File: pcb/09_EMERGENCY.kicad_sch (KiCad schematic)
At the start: 14 parts, among them K1 HF115F-1/5V-H, Q20 AO3400A

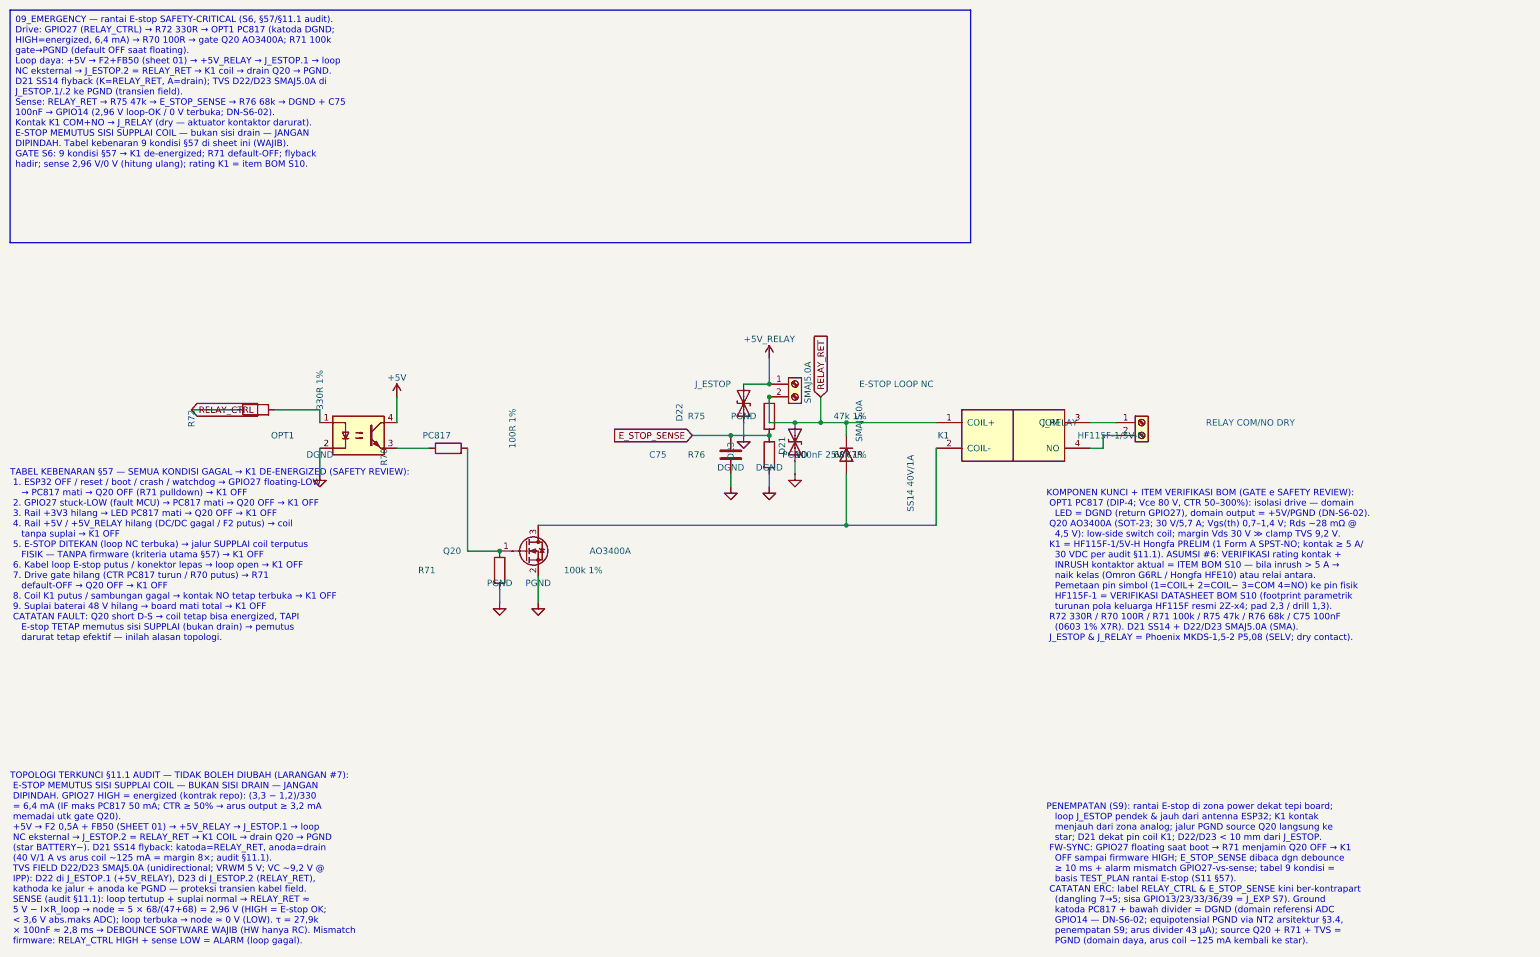
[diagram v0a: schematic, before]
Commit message: pcb: S12 relay-expansion integration + R1/R2 e-stop fixes (schematic + board)
- 09_EMERGENCY: R1 fix (active-LOW drive: R72 high-side from +3V3, OPT1 cathode
  -> RELAY_CTRL, R78 10k pull-up fail-safe) + R2 fix (inverting sense: Q21
  BSS138 + R77 100k divider + R76 revalued 10k pull-up, C75 filter; HIGH=trip
  matches GPIO14 INPUT_PULLUP contract); truth table/docs updated
- NEW 12_RELAY_EXP: F4 1.1A + FB2 -> +5V_RELAY_EXP rail, J_RELAY_EXP 2x03,
  BSS138 I2C shifters Q22/Q23 + R79/R84 4k7, TVS D24/D25 DNP, INT divider
  R82/R83 (PCF8574 module external, 0x20, active-LOW)
- root sch: sheet 12 entry (page 13); plts-custom: +5V_RELAY_EXP symbol
- pro: PWR netclass pattern for +5V_RELAY_EXP
- 01_POWER: C52 22uF->47uF 25V X5R (relay coil dip headroom)
- board: +7 nets, +14 footprints, pad re-netting, placement to 0 structural
  DRC; repaired broken hand-drawn courtyards (M1/U1/K1/J_I2C_EXP) to true
  geometry; U1 antenna keepout respected

ERC: 0 violations (13 sheets). DRC: 0 structural (courtyard/short/keepout/
clearance clean; silk/via/thermal/isolated = post-routing cleanup).
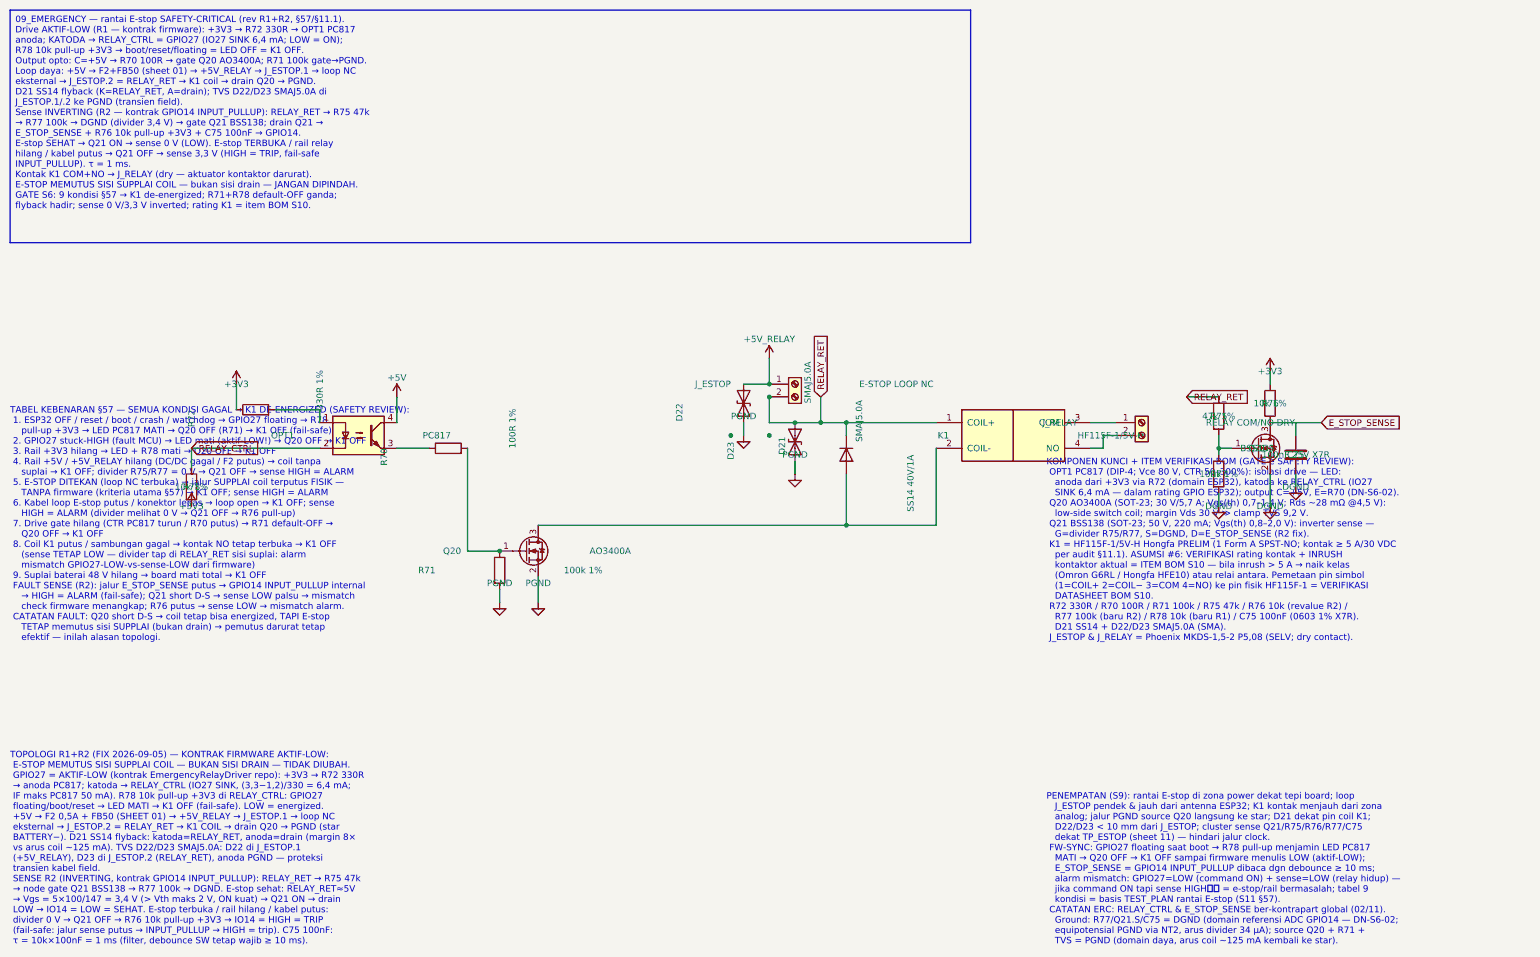
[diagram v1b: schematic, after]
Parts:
- added Q21: BSS138, Package_TO_SOT_SMD:SOT-23, symbol Transistor_FET:BSS138
- added R77: 100k 1%, Resistor_SMD:R_0603_1608Metric, symbol Device:R
- added R78: 10k 1%, Resistor_SMD:R_0603_1608Metric, symbol Device:R
- R76: value 68k 1% -> 10k 1%
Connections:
- net DGND: now also Q21.2 (S), R77.2; no longer OPT1.2, R76.2
- net E_STOP_SENSE: now also Q21.3 (D); no longer R75.2
- net RELAY_CTRL: now also OPT1.2, R78.1; no longer R72.1
- new net: Q21.1 (G), R75.2, R77.1
- new net +3V3: R72.1, R76.2, R78.2
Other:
- note added: "KOMPONEN KUNCI + ITEM VERIFIKASI BOM (GATE e SAFETY REVIEW): OPT1 PC817 (DIP-4; Vce 80 V, CTR 50–300%): isolasi drive — LED: anoda dari +3V3 via R72 (domain ESP32), katoda ke RELAY_CTRL (IO27 SINK 6,4 mA — dalam rating GPIO ESP32); output C=+5V, E=R70 (DN-S6-02). Q20 AO3400A (SOT-23; 30 V/5,7 A; Vgs(th) 0,7–1,4 V; Rds ~28 mΩ @4,5 V): low-side switch coil; margin Vds 30 V ≫ clamp TVS 9,2 V. Q21 BS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"
- note added: "PENEMPATAN (S9): rantai E-stop di zona power dekat tepi board; loop J_ESTOP pendek & jauh dari antenna ESP32; K1 kontak menjauh dari zona analog; jalur PGND source Q20 langsung ke star; D21 dekat pin coil K1; D22/D23 < 10 mm dari J_ESTOP; cluster sense Q21/R75/R76/R77/C75 dekat TP_ESTOP (sheet 11) — hindari jalur clock. FW-SYNC: GPIO27 floating saat boot → R78 pull-up menjamin LED PC817 MATI → Q2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"
- note added: "TABEL KEBENARAN §57 — SEMUA KONDISI GAGAL → K1 DE-ENERGIZED (SAFETY REVIEW): 1. ESP32 OFF / reset / boot / crash / watchdog → GPIO27 floating → R78 pull-up +3V3 → LED PC817 MATI → Q20 OFF (R71) → K1 OFF (fail-safe) 2. GPIO27 stuck-HIGH (fault MCU) → LED mati (aktif-LOW!) → Q20 OFF → K1 OFF 3. Rail +3V3 hilang → LED + R78 mati → Q20 OFF → K1 OFF 4. Rail +5V / +5V_RELAY hilang (DC/DC gagal / F2 put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"
- note added: "TOPOLOGI R1+R2 (FIX 2026-09-05) — KONTRAK FIRMWARE AKTIF-LOW: E-STOP MEMUTUS SISI SUPPLAI COIL — BUKAN SISI DRAIN — TIDAK DIUBAH. GPIO27 = AKTIF-LOW (kontrak EmergencyRelayDriver repo): +3V3 → R72 330R → anoda PC817; katoda → RELAY_CTRL (IO27 SINK, (3,3−1,2)/330 = 6,4 mA; IF maks PC817 50 mA). R78 10k pull-up +3V3 di RELAY_CTRL: GPIO27 floating/boot/reset → LED MATI → K1 OFF (fail-safe). LOW = en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"
- note removed: "KOMPONEN KUNCI + ITEM VERIFIKASI BOM (GATE e SAFETY REVIEW): OPT1 PC817 (DIP-4; Vce 80 V, CTR 50–300%): isolasi drive — domain LED = DGND (return GPIO27), domain output = +5V/PGND (DN-S6-02). Q20 AO3400A (SOT-23; 30 V/5,7 A; Vgs(th) 0,7–1,4 V; Rds ~28 mΩ @ 4,5 V): low-side switch coil; margin Vds 30 V ≫ clamp TVS 9,2 V. K1 = HF115F-1/5V-H Hongfa PRELIM (1 Form A SPST-NO; kontak ≥ 5 A/ 30 VDC per 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"
- note removed: "PENEMPATAN (S9): rantai E-stop di zona power dekat tepi board; loop J_ESTOP pendek & jauh dari antenna ESP32; K1 kontak menjauh dari zona analog; jalur PGND source Q20 langsung ke star; D21 dekat pin coil K1; D22/D23 < 10 mm dari J_ESTOP. FW-SYNC: GPIO27 floating saat boot → R71 menjamin Q20 OFF → K1 OFF sampai firmware HIGH; E_STOP_SENSE dibaca dgn debounce ≥ 10 ms + alarm mismatch GPIO27-vs-sen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"
- note removed: "TABEL KEBENARAN §57 — SEMUA KONDISI GAGAL → K1 DE-ENERGIZED (SAFETY REVIEW): 1. ESP32 OFF / reset / boot / crash / watchdog → GPIO27 floating-LOW → PC817 mati → Q20 OFF (R71 pulldown) → K1 OFF 2. GPIO27 stuck-LOW (fault MCU) → PC817 mati → Q20 OFF → K1 OFF 3. Rail +3V3 hilang → LED PC817 mati → Q20 OFF → K1 OFF 4. Rail +5V / +5V_RELAY hilang (DC/DC gagal / F2 putus) → coil tanpa suplai → K1 OFF 5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"
- note removed: "TOPOLOGI TERKUNCI §11.1 AUDIT — TIDAK BOLEH DIUBAH (LARANGAN #7): E-STOP MEMUTUS SISI SUPPLAI COIL — BUKAN SISI DRAIN — JANGAN DIPINDAH. GPIO27 HIGH = energized (kontrak repo): (3,3 − 1,2)/330 = 6,4 mA (IF maks PC817 50 mA; CTR ≥ 50% → arus output ≥ 3,2 mA memadai utk gate Q20). +5V → F2 0,5A + FB50 (SHEET 01) → +5V_RELAY → J_ESTOP.1 → loop NC eksternal → J_ESTOP.2 = RELAY_RET → K1 COIL → drain Q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"
